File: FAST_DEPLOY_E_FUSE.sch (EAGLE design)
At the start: 183 parts, among them IC1 LTC4222CUH#PBF, IC2 LTC4222CUH#PBF, IC3 ADM1177-2ARMZ-R7, IC4 ADM1177-2ARMZ-R7, IC5 MCP1792T-3302H_CB, IC6 74HC4852BQ,115, M1 NTLUS4C12NTAG, M2 NTLUS4C12NTAG, M3 NTLUS4C12NTAG, M4 NTLUS4C12NTAG, M5 NTLUS4C12NTAG, M6 NTLUS4C12NTAG

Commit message: Needs final labeling touch ups
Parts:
- added TP55, TP56, TP57, TP58, TP59, TP60, TP61, TP62: S1751-46R, SamacSys_Parts:S1751-46R
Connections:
- net GND: now also TP55.1, TP56.1, TP57.1, TP58.1, TP59.1, TP60.1, TP61.1, TP62.1
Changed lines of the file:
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@@
 <part name="JP21" library="pinhead" library_urn="urn:adsk.eagle:library:325" deviceset="PINHD-1X2" device="" package3d_urn="urn:adsk.eagle:package:22435/2"/>
 <part name="JP22" library="pinhead" library_urn="urn:adsk.eagle:library:325" deviceset="PINHD-1X5" device="" package3d_urn="urn:adsk.eagle:package:22469/2"/>
+<part name="TP55" library="SamacSys_Parts" library_urn="urn:adsk.eagle:library:31941355" deviceset="S1751-46R" device="" package3d_urn="urn:adsk.eagle:package:31969460/2"/>
+<part name="TP56" library="SamacSys_Parts" library_urn="urn:adsk.eagle:library:31941355" deviceset="S1751-46R" device="" package3d_urn="urn:adsk.eagle:package:31969460/2"/>
+<part name="TP57" library="SamacSys_Parts" library_urn="urn:adsk.eagle:library:31941355" deviceset="S1751-46R" device="" package3d_urn="urn:adsk.eagle:package:31969460/2"/>
+<part name="TP58" library="SamacSys_Parts" library_urn="urn:adsk.eagle:library:31941355" deviceset="S1751-46R" device="" package3d_urn="urn:adsk.eagle:package:31969460/2"/>
+<part name="TP59" library="SamacSys_Parts" library_urn="urn:adsk.eagle:library:31941355" deviceset="S1751-46R" device="" package3d_urn="urn:adsk.eagle:package:31969460/2"/>
+<part name="TP60" library="SamacSys_Parts" library_urn="urn:adsk.eagle:library:31941355" deviceset="S1751-46R" device="" package3d_urn="urn:adsk.eagle:package:31969460/2"/>
+<part name="TP61" library="SamacSys_Parts" library_urn="urn:adsk.eagle:library:31941355" deviceset="S1751-46R" device="" package3d_urn="urn:adsk.eagle:package:31969460/2"/>
+<part name="TP62" library="SamacSys_Parts" library_urn="urn:adsk.eagle:library:31941355" deviceset="S1751-46R" device="" package3d_urn="urn:adsk.eagle:package:31969460/2"/>
 </parts>
 <sheets>
@@
 <attribute name="VALUE" x="41.91" y="17.78" size="1.778" layer="96" rot="R180"/>
 </instance>
+<instance part="TP55" gate="G$1" x="73.66" y="66.04" smashed="yes" rot="R270">
+<attribute name="NAME" x="81.28" y="49.53" size="1.778" layer="95" rot="R270" align="center-left"/>
+<attribute name="VALUE" x="78.74" y="49.53" size="1.778" layer="96" rot="R270" align="center-left"/>
+</instance>
+<instance part="TP56" gate="G$1" x="88.9" y="66.04" smashed="yes" rot="R270">
+<attribute name="NAME" x="96.52" y="49.53" size="1.778" layer="95" rot="R270" align="center-left"/>
+<attribute name="VALUE" x="93.98" y="49.53" size="1.778" layer="96" rot="R270" align="center-left"/>
+</instance>
+<instance part="TP57" gate="G$1" x="104.14" y="66.04" smashed="yes" rot="R270">
+<attribute name="NAME" x="111.76" y="49.53" size="1.778" layer="95" rot="R270" align="center-left"/>
+<attribute name="VALUE" x="109.22" y="49.53" size="1.778" layer="96" rot="R270" align="center-left"/>
+</instance>
+<instance part="TP58" gate="G$1" x="119.38" y="66.04" smashed="yes" rot="R270">
+<attribute name="NAME" x="127" y="49.53" size="1.778" layer="95" rot="R270" align="center-left"/>
+<attribute name="VALUE" x="124.46" y="49.53" size="1.778" layer="96" rot="R270" align="center-left"/>
+</instance>
+<instance part="TP59" gate="G$1" x="73.66" y="30.48" smashed="yes" rot="R270">
+<attribute name="NAME" x="81.28" y="13.97" size="1.778" layer="95" rot="R270" align="center-left"/>
+<attribute name="VALUE" x="78.74" y="13.97" size="1.778" layer="96" rot="R270" align="center-left"/>
+</instance>
+<instance part="TP60" gate="G$1" x="88.9" y="30.48" smashed="yes" rot="R270">
+<attribute name="NAME" x="96.52" y="13.97" size="1.778" layer="95" rot="R270" align="center-left"/>
+<attribute name="VALUE" x="93.98" y="13.97" size="1.778" layer="96" rot="R270" align="center-left"/>
+</instance>
+<instance part="TP61" gate="G$1" x="104.14" y="30.48" smashed="yes" rot="R270">
+<attribute name="NAME" x="111.76" y="13.97" size="1.778" layer="95" rot="R270" align="center-left"/>
+<attribute name="VALUE" x="109.22" y="13.97" size="1.778" layer="96" rot="R270" align="center-left"/>
+</instance>
+<instance part="TP62" gate="G$1" x="119.38" y="30.48" smashed="yes" rot="R270">
+<attribute name="NAME" x="127" y="13.97" size="1.778" layer="95" rot="R270" align="center-left"/>
+<attribute name="VALUE" x="124.46" y="13.97" size="1.778" layer="96" rot="R270" align="center-left"/>
+</instance>
 </instances>
 <busses>
@@
 </segment>
 </net>
+<net name="GND" class="0">
+<segment>
+<pinref part="TP55" gate="G$1" pin="1"/>
+<wire x1="73.66" y1="66.04" x2="73.66" y2="71.12" width="0.1524" layer="91"/>
+<label x="73.66" y="68.58" size="1.778" layer="95" rot="R90"/>
+</segment>
+<segment>
+<pinref part="TP56" gate="G$1" pin="1"/>
+<wire x1="88.9" y1="66.04" x2="88.9" y2="71.12" width="0.1524" layer="91"/>
+<label x="88.9" y="68.58" size="1.778" layer="95" rot="R90"/>
+</segment>
+<segment>
+<pinref part="TP57" gate="G$1" pin="1"/>
+<wire x1="104.14" y1="66.04" x2="104.14" y2="71.12" width="0.1524" layer="91"/>
+<label x="104.14" y="68.58" size="1.778" layer="95" rot="R90"/>
+</segment>
+<segment>
+<pinref part="TP58" gate="G$1" pin="1"/>
+<wire x1="119.38" y1="66.04" x2="119.38" y2="71.12" width="0.1524" layer="91"/>
+<label x="119.38" y="68.58" size="1.778" layer="95" rot="R90"/>
+</segment>
+<segment>
+<pinref part="TP59" gate="G$1" pin="1"/>
+<wire x1="73.66" y1="30.48" x2="73.66" y2="35.56" width="0.1524" layer="91"/>
+<label x="73.66" y="33.02" size="1.778" layer="95" rot="R90"/>
+</segment>
+<segment>
+<pinref part="TP60" gate="G$1" pin="1"/>
+<wire x1="88.9" y1="30.48" x2="88.9" y2="35.56" width="0.1524" layer="91"/>
+<label x="88.9" y="33.02" size="1.778" layer="95" rot="R90"/>
+</segment>
+<segment>
+<pinref part="TP61" gate="G$1" pin="1"/>
+<wire x1="104.14" y1="30.48" x2="104.14" y2="35.56" width="0.1524" layer="91"/>
+<label x="104.14" y="33.02" size="1.778" layer="95" rot="R90"/>
+</segment>
+<segment>
+<pinref part="TP62" gate="G$1" pin="1"/>
+<wire x1="119.38" y1="30.48" x2="119.38" y2="35.56" width="0.1524" layer="91"/>
+<label x="119.38" y="33.02" size="1.778" layer="95" rot="R90"/>
+</segment>
+</net>

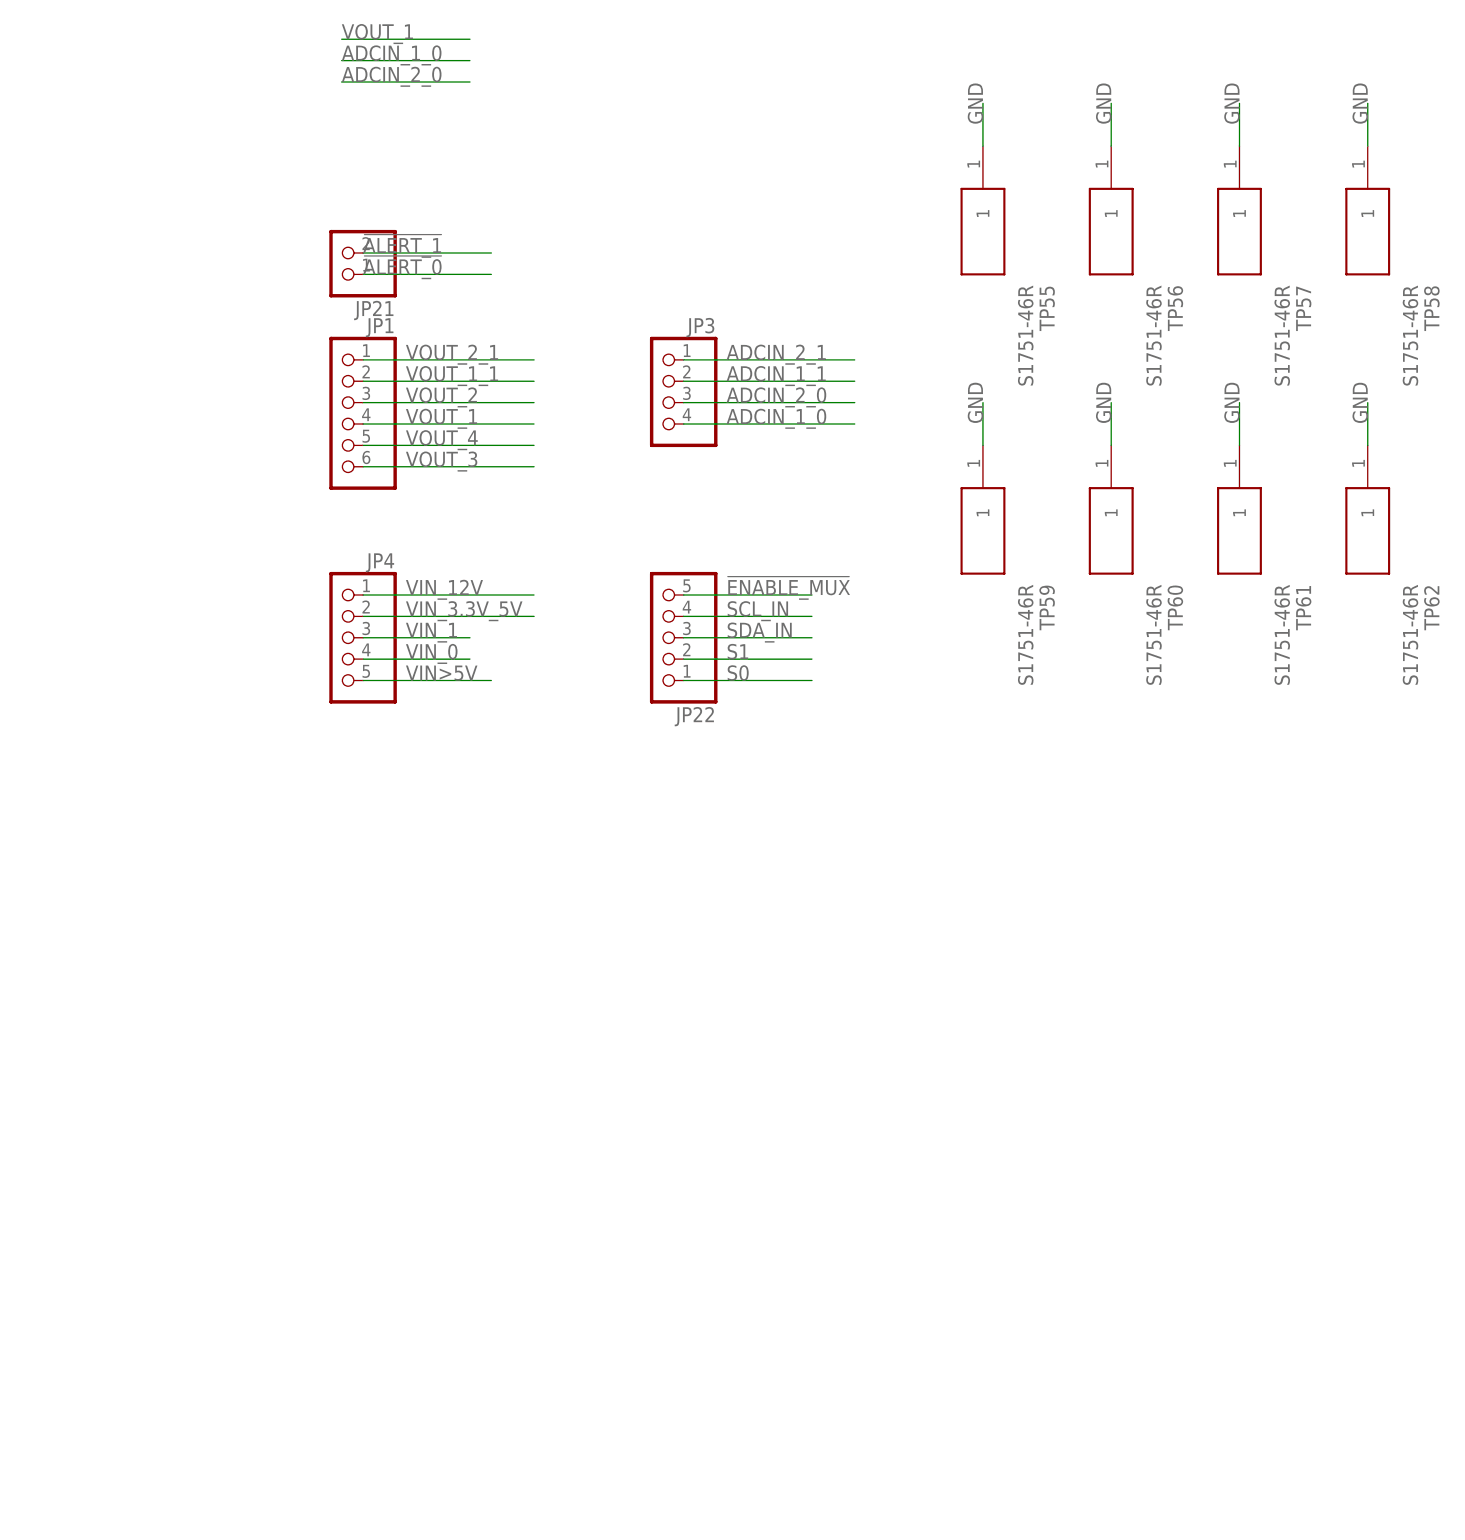
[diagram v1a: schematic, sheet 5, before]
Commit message: Added power leds and labels, -Ready for manufacturing
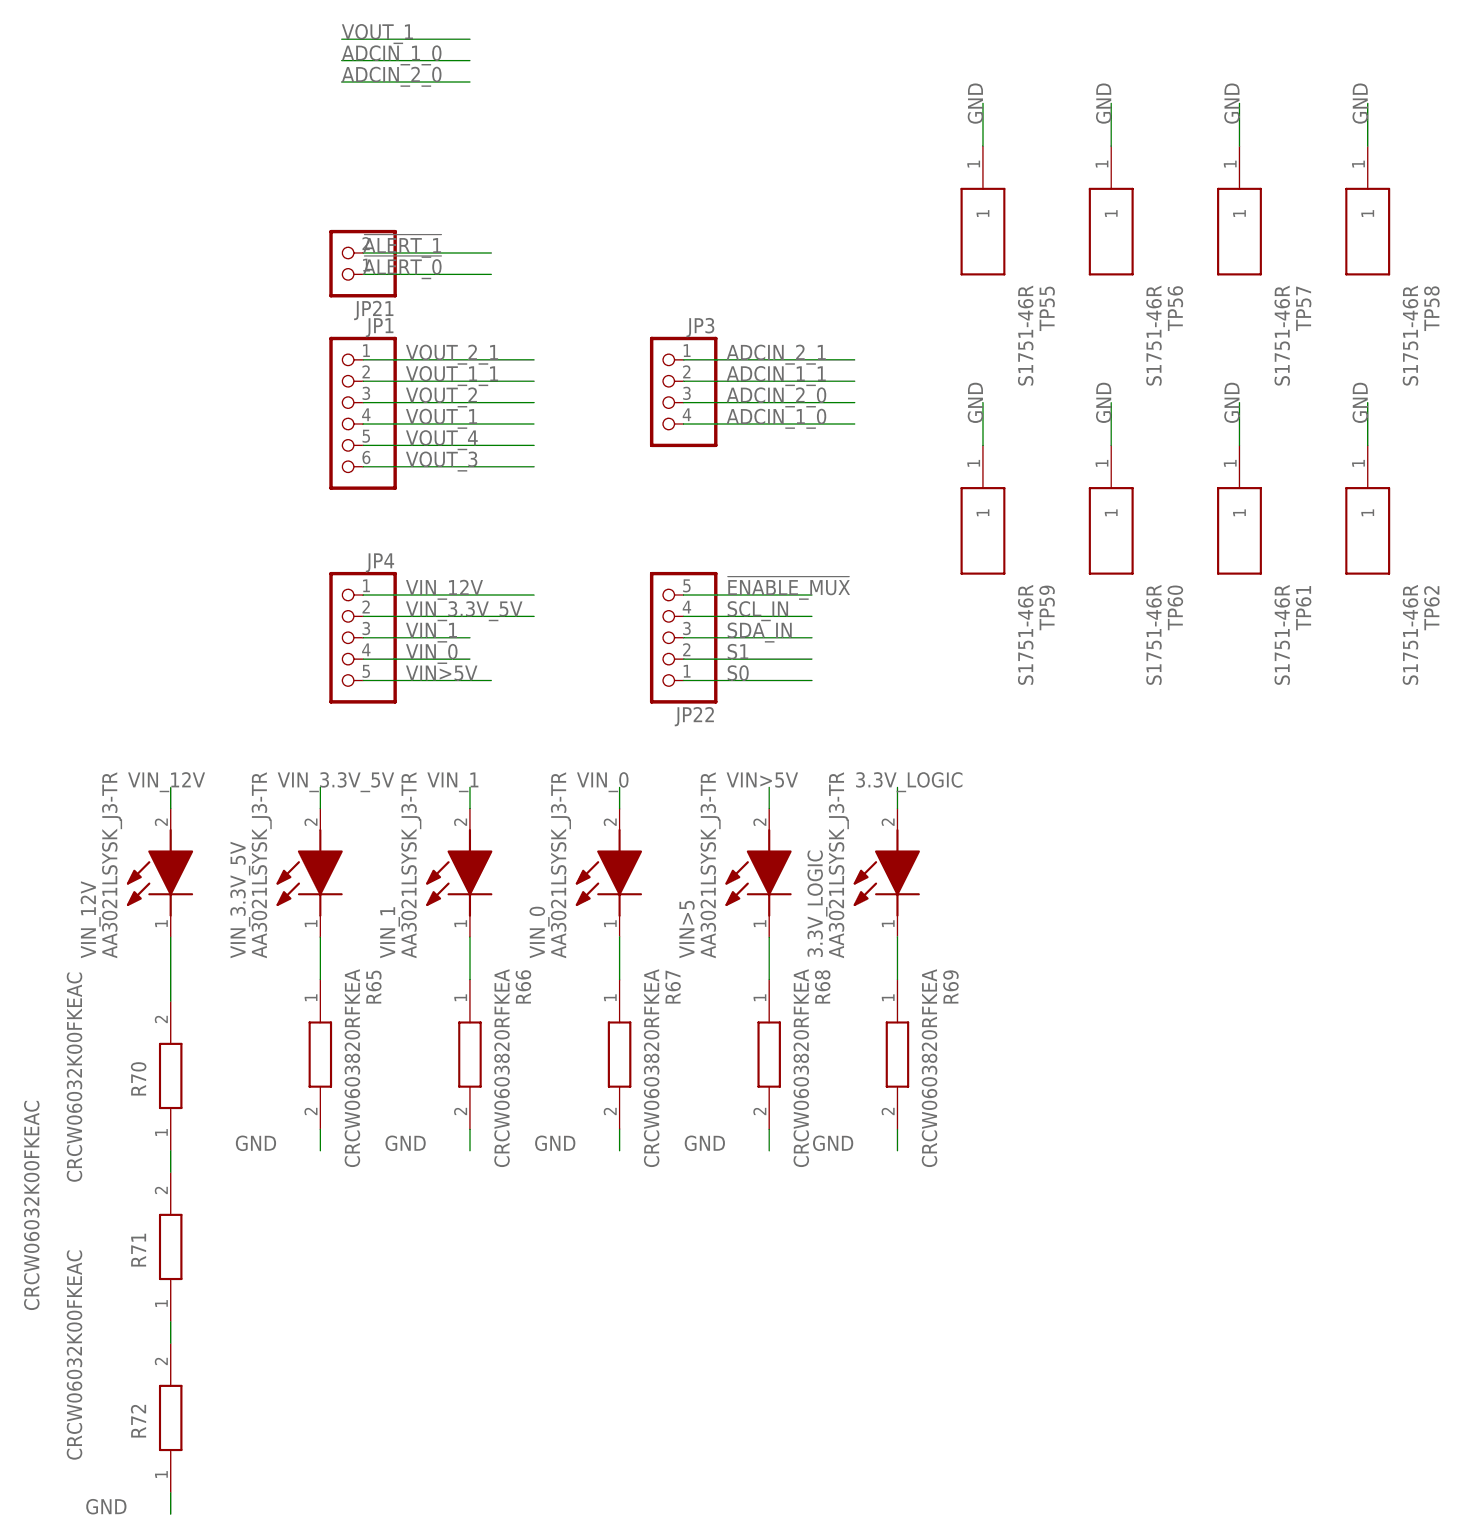
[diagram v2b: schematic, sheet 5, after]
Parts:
- added 3.3V_LOGIC, VIN>5, VIN_0, VIN_1, VIN_12V, VIN_3.3V_5V: AA3021LSYSK_J3-TR, SamacSys_Parts:AA3021LSYSK_J3-TR
- added R65, R66, R67, R68, R69: CRCW0603820RFKEA, SamacSys_Parts:CRCW0603820RFKEA
- added R70, R71, R72: CRCW06032K00FKEAC, SamacSys_Parts:CRCW06032K00FKEAC
- renumbered LED1 to !ALERT0, LED10 to SDA_IN, LED11 to 3_SCL, LED12 to 3_SDA, LED13 to !EN_MUX, LED14 to S0, LED15 to S1, LED2 to 0_SCL, LED3 to 0_SDA, LED4 to !ALERT1, LED5 to 1_SCL, LED6 to 1_SDA, LED7 to SCL_IN, LED8 to 2_SCL, LED9 to SDA_2
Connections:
- net LED_1 renamed !ALERT0
- net LED_10 renamed SDA_INPUT
- net LED_11 renamed 3_SCL
- net LED_12 renamed 3_SDA
- net LED_13 renamed !EN_MUX
- net LED_14 renamed S0_IN
- net LED_15 renamed S1_IN
- net LED_2 renamed 0_SCL
- net LED_3 renamed 0_SDA
- net LED_4 renamed !ALERT1
- net LED_5 renamed 1_SCL
- net LED_6 renamed 1_SDA
- net LED_7 renamed SCL_INPUT
- net LED_8 renamed S_SDA
- net LED_9 renamed 2_SDA
- new net N$1: R70.1, R71.2
- new net N$2: R71.1, R72.2
- new net N$3: R70.2, VIN_12V.K
- new net N$4: R65.1, VIN_3.3V_5V.K
- new net N$5: R66.1, VIN_1.K
- new net N$6: R67.1, VIN_0.K
- new net N$7: R68.1, VIN>5.K
- new net N$8: 3.3V_LOGIC.K, R69.1
- net 3.3V_LOGIC: now also 3.3V_LOGIC.A
- net GND: now also R65.2, R66.2, R67.2, R68.2, R69.2, R72.1
- net VIN>5V: now also VIN>5.A
- net VIN_0: now also VIN_0.A
- net VIN_1: now also VIN_1.A
- net VIN_12V: now also VIN_12V.A
- net VIN_3.3V_5V: now also VIN_3.3V_5V.A
